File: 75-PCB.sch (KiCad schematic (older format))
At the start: 186 parts

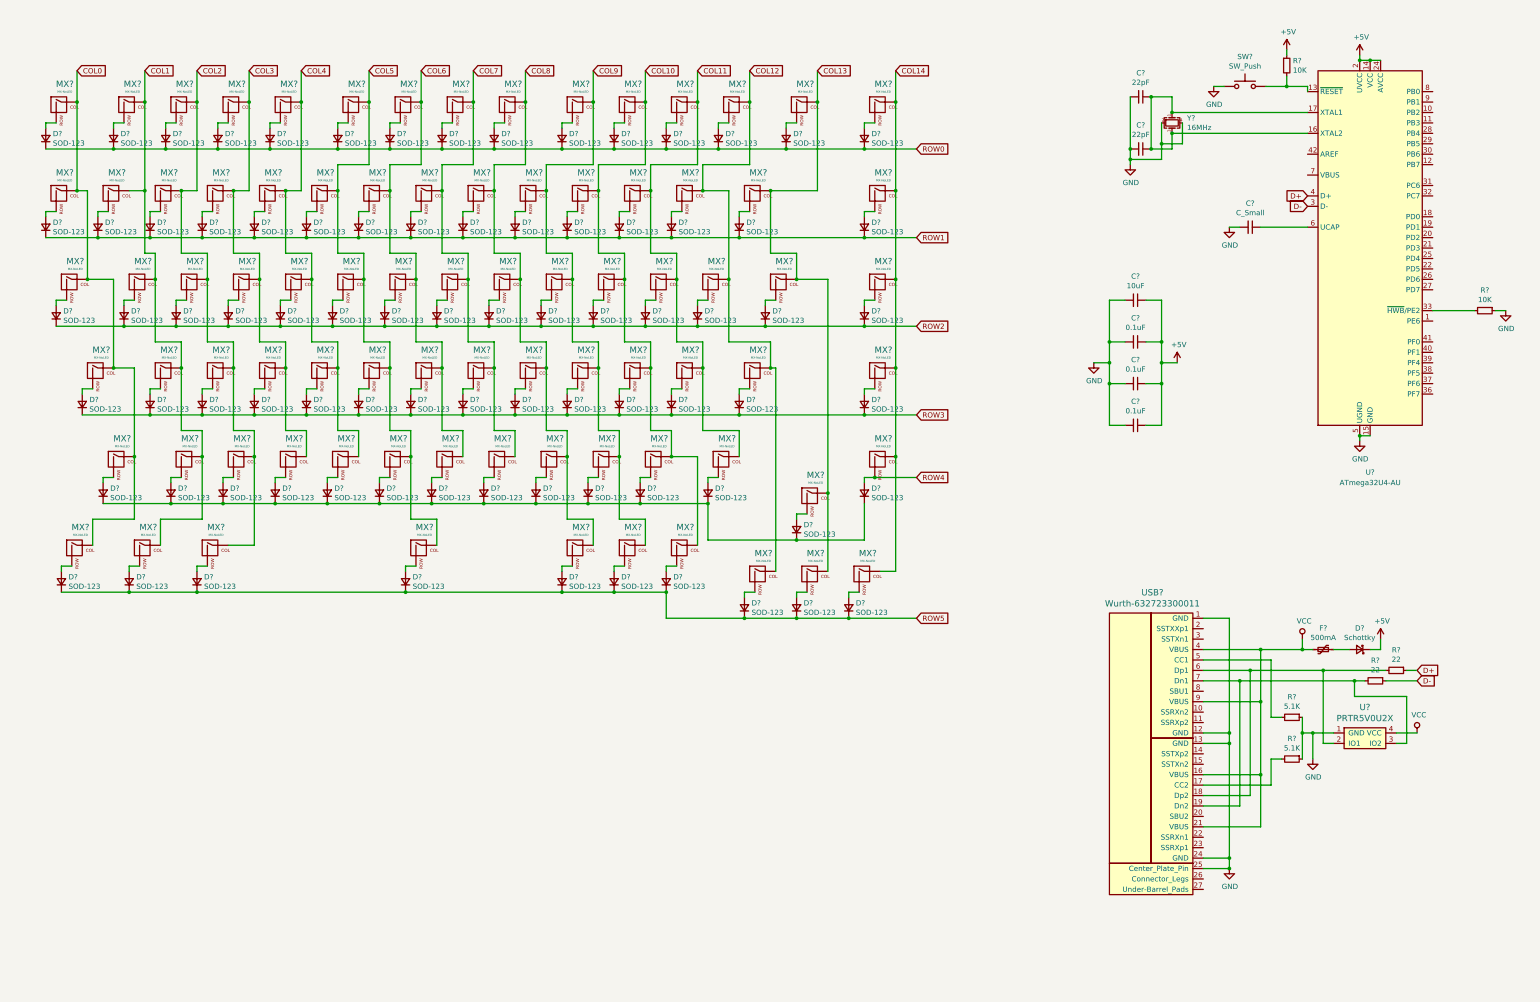
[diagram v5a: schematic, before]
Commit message: Changed switches to support LEDs
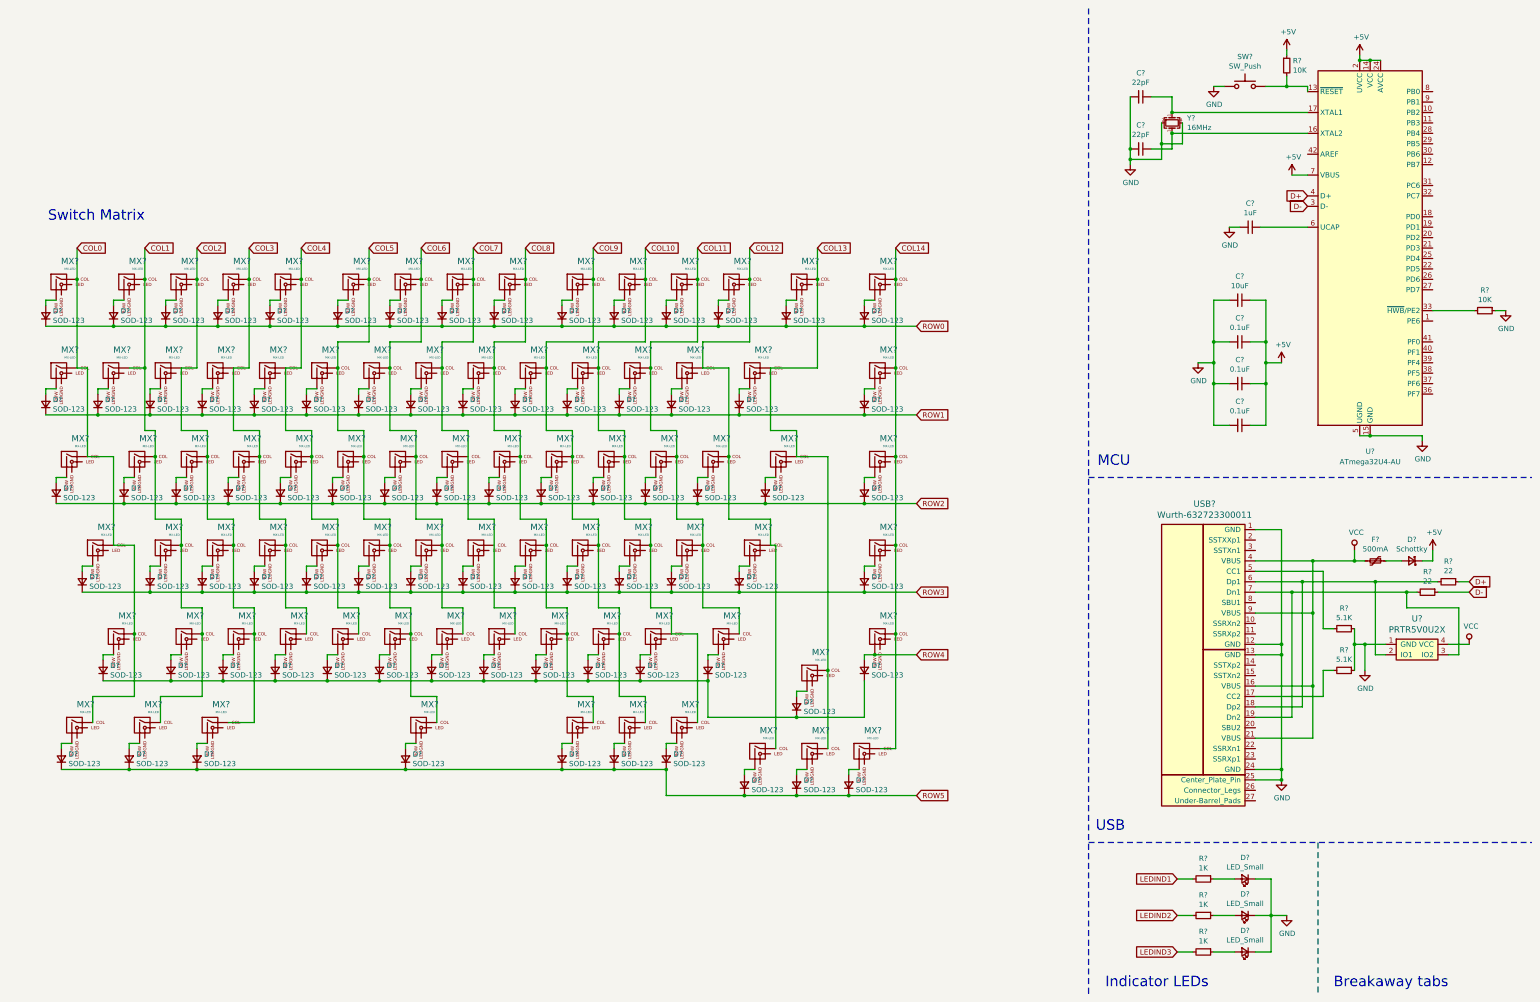
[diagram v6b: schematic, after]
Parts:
- removed MX? (x83): MX-NoLED, symbol MX_Alps_Hybrid:MX-NoLED
- added D? (x3): LED_Small, symbol Device:LED_Small
- added MX? (x83): MX-LED, symbol MX_Alps_Hybrid:MX-LED
- added R? (x3): 1K, symbol Device:R_Small
- C?: value C_Small -> 1uF
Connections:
- net +5V: now also U?.7 (VBUS)
- net COL0: now also MX?.1 (COL), MX?.1 (COL), MX?.1 (COL), MX?.1 (COL), MX?.1 (COL), MX?.1 (COL)
- net COL1: now also MX?.1 (COL), MX?.1 (COL), MX?.1 (COL), MX?.1 (COL), MX?.1 (COL), MX?.1 (COL)
- net COL10: now also MX?.1 (COL), MX?.1 (COL), MX?.1 (COL), MX?.1 (COL), MX?.1 (COL), MX?.1 (COL)
- net COL11: now also MX?.1 (COL), MX?.1 (COL), MX?.1 (COL), MX?.1 (COL), MX?.1 (COL)
- net COL12: now also MX?.1 (COL), MX?.1 (COL), MX?.1 (COL), MX?.1 (COL), MX?.1 (COL)
- net COL13: now also MX?.1 (COL), MX?.1 (COL), MX?.1 (COL), MX?.1 (COL), MX?.1 (COL)
- net COL14: now also MX?.1 (COL), MX?.1 (COL), MX?.1 (COL), MX?.1 (COL), MX?.1 (COL), MX?.1 (COL)
- net COL2: now also MX?.1 (COL), MX?.1 (COL), MX?.1 (COL), MX?.1 (COL), MX?.1 (COL), MX?.1 (COL)
- net COL3: now also MX?.1 (COL), MX?.1 (COL), MX?.1 (COL), MX?.1 (COL), MX?.1 (COL)
- net COL4: now also MX?.1 (COL), MX?.1 (COL), MX?.1 (COL), MX?.1 (COL), MX?.1 (COL)
- net COL5: now also MX?.1 (COL), MX?.1 (COL), MX?.1 (COL), MX?.1 (COL), MX?.1 (COL), MX?.1 (COL)
- net COL6: now also MX?.1 (COL), MX?.1 (COL), MX?.1 (COL), MX?.1 (COL), MX?.1 (COL)
- net COL7: now also MX?.1 (COL), MX?.1 (COL), MX?.1 (COL)
- net COL8: now also MX?.1 (COL), MX?.1 (COL), MX?.1 (COL), MX?.1 (COL), MX?.1 (COL), MX?.1 (COL)
- net COL9: now also MX?.1 (COL), MX?.1 (COL), MX?.1 (COL), MX?.1 (COL), MX?.1 (COL), MX?.1 (COL)
- net GND: now also D?.1 (K), D?.1 (K), D?.1 (K)
- net ROW4: now also MX?.2 (ROW)
- net at C?.1, U?.16 (XTAL2), Y?.3: no longer C?.1, U?.17 (XTAL1), Y?.1
- net at D?.2 (A): now also MX?.2 (ROW) (x82)
- new net: C?.1, U?.17 (XTAL1), Y?.1
- new net: D?.2 (A), R?.1 (x3)
- new net LEDIND1: R?.2
- new net LEDIND2: R?.2
- new net LEDIND3: R?.2
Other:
- note added: "Breakaway tabs\n"
- note added: "Indicator LEDs"
- note added: "MCU\n"
- note added: "Switch Matrix\n"
- note added: "USB\n"
- moved on the sheet: C?, D?, F?, R?, U?, USB?

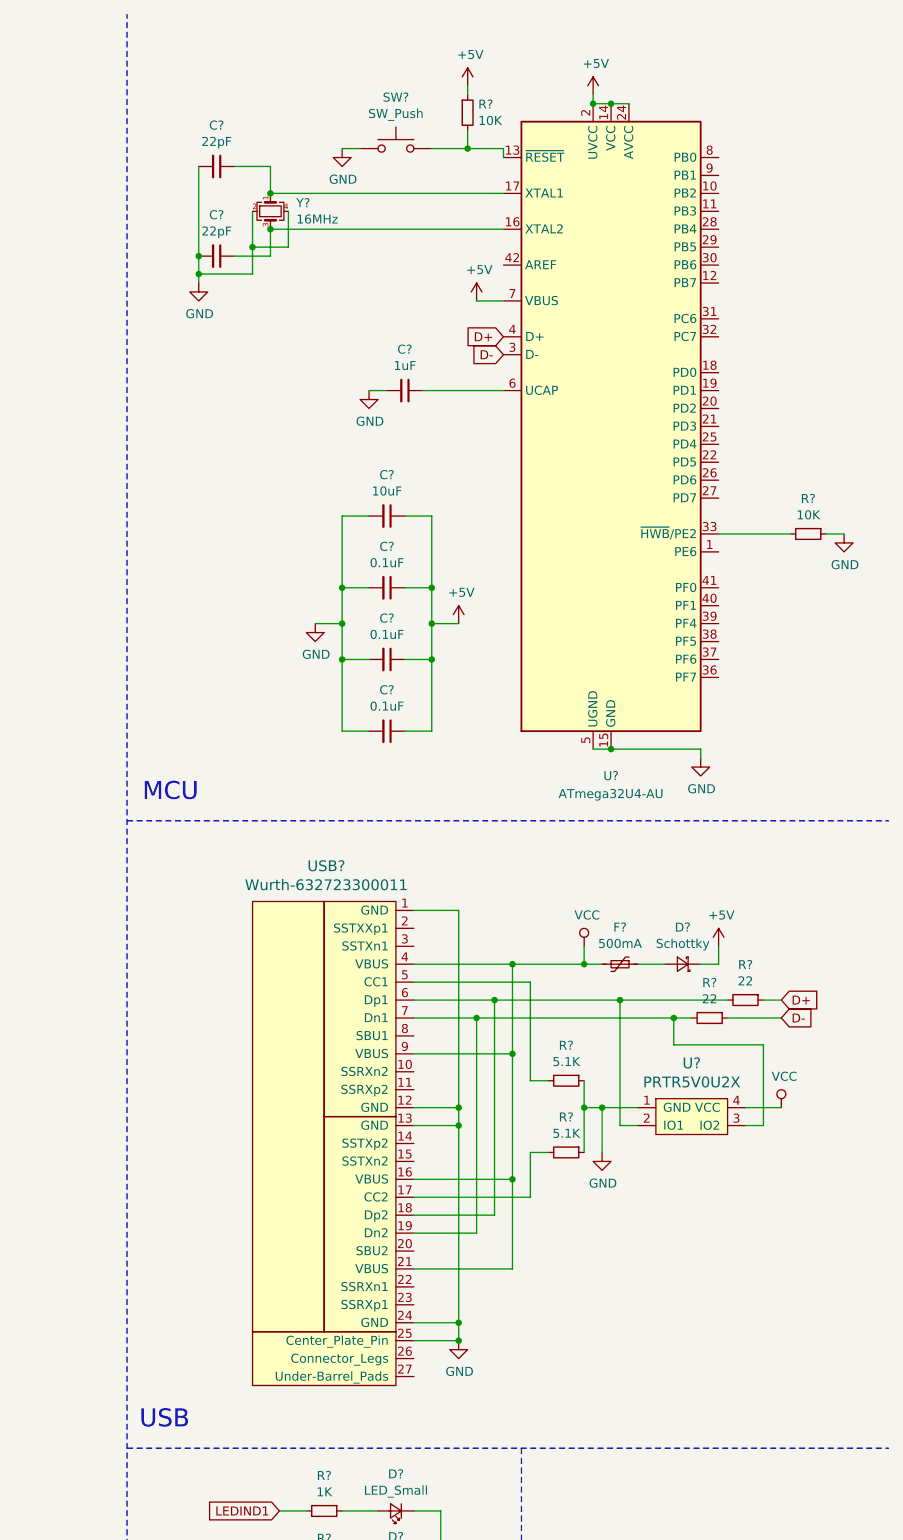
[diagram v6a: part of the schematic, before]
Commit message: Changed MCU from ATmega32U4 to AT90USB1286 for more pins
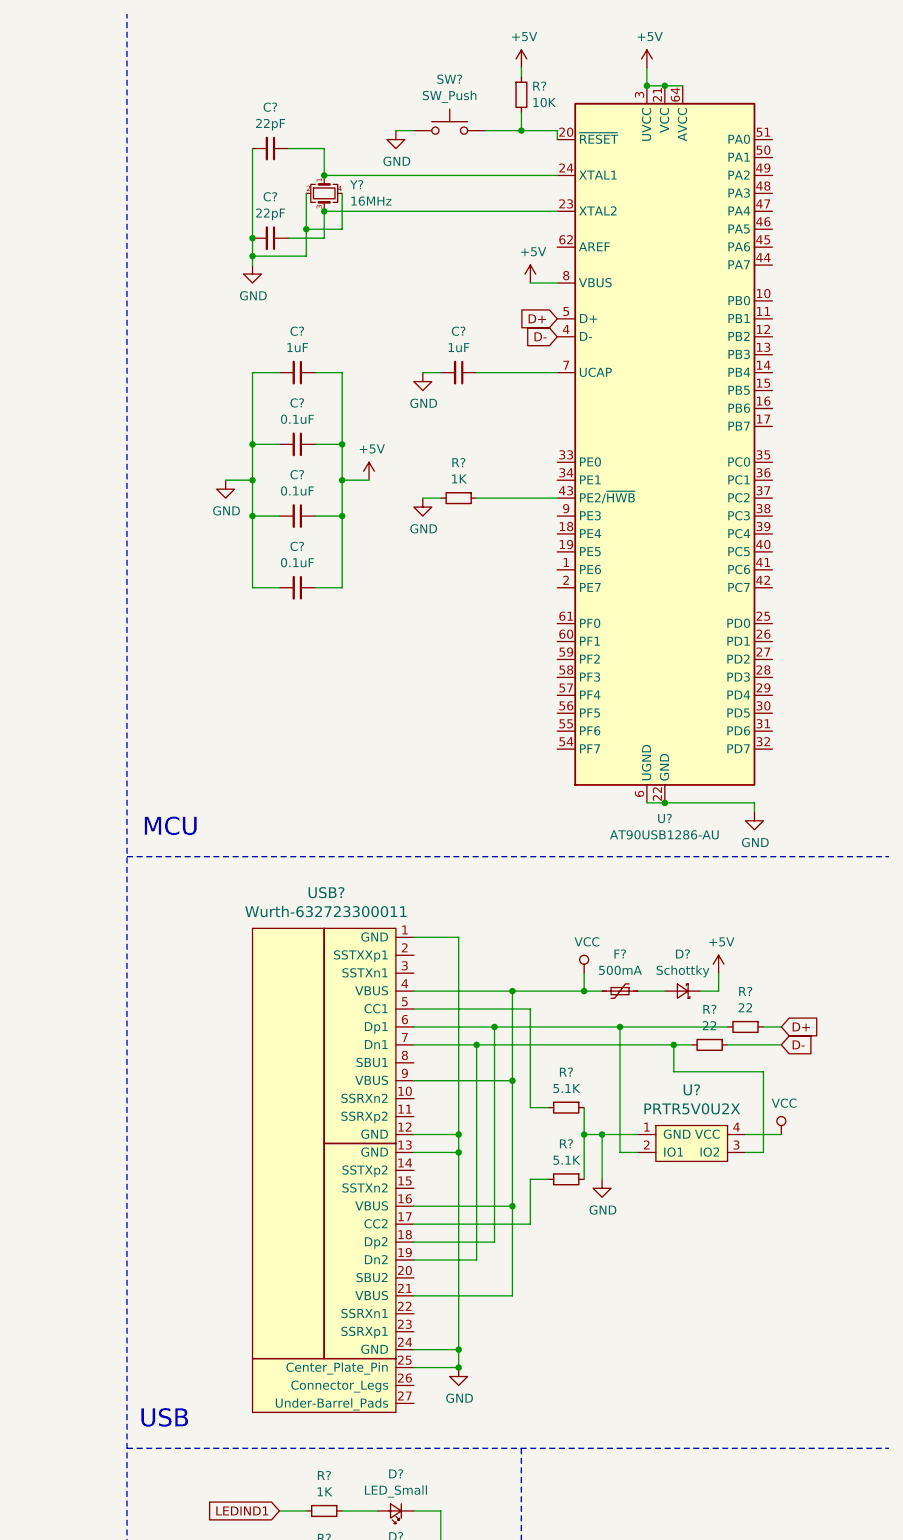
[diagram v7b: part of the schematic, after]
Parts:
- removed C?: 1uF, symbol Device:C_Small
- removed C? (x2): 22pF, symbol Device:C_Small
- removed R? (x2): 10K, symbol Device:R_Small
- removed SW?: SW_Push, symbol Switch:SW_Push
- removed U?: ATmega32U4-AU, Package_QFP:TQFP-44_10x10mm_P0.8mm, symbol MCU_Microchip_ATmega:ATmega32U4-AU
- removed Y?: 16MHz, symbol Device:Crystal_GND24_Small
- added C? (x2): 22pF, symbol Device:C_Small
- added C?: 1uF, symbol Device:C_Small
- added R?: 1K, symbol Device:R_Small
- added R?: 10K, symbol Device:R_Small
- added SW?: SW_Push, symbol Switch:SW_Push
- added U?: AT90USB1286-AU, Package_QFP:TQFP-64_14x14mm_P0.8mm, symbol MCU_Microchip_AVR:AT90USB1286-AU
- added Y?: 16MHz, symbol Device:Crystal_GND24_Small
- C?: value 10uF -> 1uF
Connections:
- net +5V: now also R?.1, U?.21 (VCC), U?.3 (UVCC), U?.52 (VCC), U?.64 (AVCC), U?.8 (VBUS)
- net D+: now also U?.5 (D+)
- net D-: now also U?.4 (D-)
- net GND: now also C?.2, C?.2, C?.2, R?.2, SW?.1, U?.22 (GND), U?.53 (GND), U?.6 (UGND), U?.63 (GND), Y?.2, Y?.4
- new net: R?.2, SW?.2, U?.20 (~RESET)
- new net: C?.1, U?.23 (XTAL2), Y?.3
- new net: C?.1, U?.24 (XTAL1), Y?.1
- new net: R?.1, U?.43 (PE2/~HWB)
- new net: C?.1, U?.7 (UCAP)
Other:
- moved on the sheet: C?, D?, F?, R?, U?, USB?
